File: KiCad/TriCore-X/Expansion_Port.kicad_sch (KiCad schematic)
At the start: 0 parts

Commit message: feat : add some Expansion Ports (work in progress)
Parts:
- added J2: 877159106, 877159106:CONN_87715-9106_MOL, symbol 877159106:877159106
- added J3: LPJG0926HENL, LPJG0926HENL:LINK-PP_LPJG0926HENL, symbol LPJG0926HENL:LPJG0926HENL
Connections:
- new net: J3.4 (CT), J3.5 (CT)
- new net: J3.S1 (SHIELD), J3.S2 (SHIELD)
- new net +12V: J2.A2, J2.A3, J2.B1, J2.B2, J2.B3
- new net GND: J2.A4, J2.B4

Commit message: refactor: change core MCU to STM32H723 and add LPDDR4/HDMI support
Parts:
- removed J3: LPJG0926HENL, LPJG0926HENL:LINK-PP_LPJG0926HENL, symbol LPJG0926HENL:LPJG0926HENL
- added D3: ESD224DQAR, ESD224DQAR:USON-10_L2.5-W1.0-P0.50-BL, symbol ESD224DQAR:ESD224DQAR
- added J3: HDMI_A, Connector_Video:HDMI_A_Molex_208658-1001_Horizontal, symbol Connector:HDMI_A
- added U1: RK3568B2, RK3568B2:BGA636C65P28X28_1900X1900X111, symbol RK3568B2:RK3568B2
- added U6: JFM38U1B-B313-4F, JFM38U1B-B313-4F:RJ45-TH_JFM38U11-B31X-4F, symbol JFM38U1B-B313-4F:JFM38U1B-B313-4F
- added U9: TPD12S016RKTR, TPD12S016RKTR:IC_TPD12S016RKTR, symbol TPD12S016RKTR:TPD12S016RKTR
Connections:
- net GND: now also U6.13 (GND), U6.16 (GND_DRAIN), U6.28 (GND), U6.4 (GND), U6.7 (GND_DRAIN), U9.13 (GND), U9.18 (GND), U9.5 (GND)
- new net HDMI_TX_AVDD_0V9: U1.V17 (HDMI_TX_AVDD_0V9), U1.V18 (HDMI_TX_AVDD_0V9)
- no-connect marks 0 -> 8

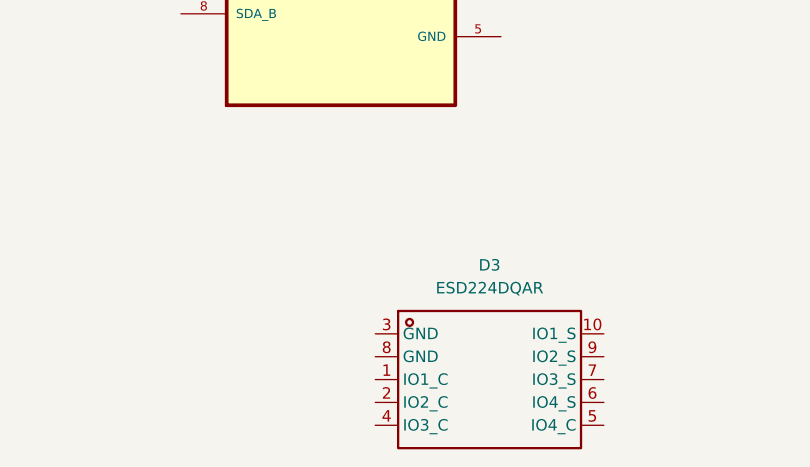
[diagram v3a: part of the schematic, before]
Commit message: feat: complete schematic for RK809-5 PMIC peripheral circuits
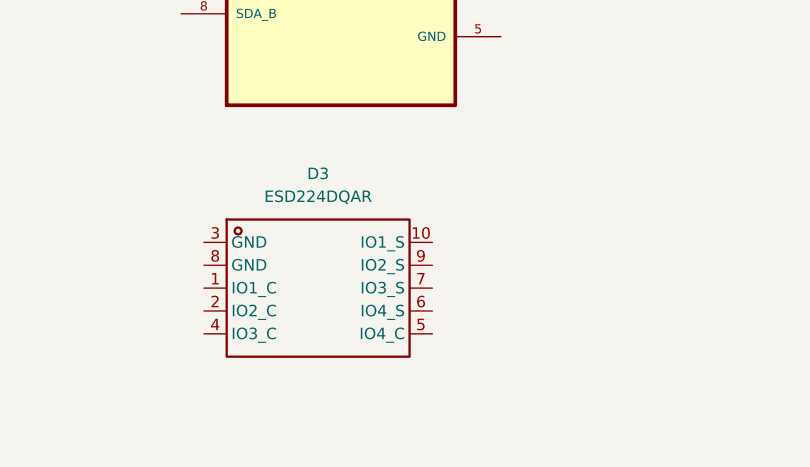
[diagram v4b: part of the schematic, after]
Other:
- moved on the sheet: D3
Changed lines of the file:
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@@
 	(symbol
 		(lib_id "ESD224DQAR:ESD224DQAR")
-		(at 466.09 138.43 0)
+		(at 447.04 128.27 0)
 		(unit 1)
 		(exclude_from_sim no)
@@
 		(fields_autoplaced yes)
 		(property "Reference" "D3"
-			(at 478.79 130.81 0)
+			(at 459.74 120.65 0)
 			(effects
 				(font
@@
 		)
 		(property "Value" "ESD224DQAR"
-			(at 478.79 133.35 0)
+			(at 459.74 123.19 0)
 			(effects
 				(font
@@
 		)
 		(property "Footprint" "ESD224DQAR:USON-10_L2.5-W1.0-P0.50-BL"
-			(at 478.79 156.21 0)
+			(at 459.74 146.05 0)
 			(effects
 				(font
@@
 		)
 		(property "Datasheet" ""
-			(at 466.09 138.43 0)
+			(at 447.04 128.27 0)
 			(effects
 				(font
@@
 		)
 		(property "Description" "ESD224DQAR"
-			(at 466.09 138.43 0)
+			(at 447.04 128.27 0)
 			(effects
 				(font
@@
 		)
 		(property "Manufacturer" "TI(德州仪器)"
-			(at 478.79 158.75 0)
+			(at 459.74 148.59 0)
 			(effects
 				(font
@@
 		)
 		(property "LCSC Part" "C1981316"
-			(at 478.79 161.29 0)
+			(at 459.74 151.13 0)
 			(effects
 				(font

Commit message: refactor: update schematic components and library references, including STM32H743 and new power symbols
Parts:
- removed J3: HDMI_A, Connector_Video:HDMI_A_Molex_208658-1001_Horizontal, symbol Connector:HDMI_A
- removed U1: RK3568B2, RK3568B2:BGA636C65P28X28_1900X1900X111, symbol RK3568B2:RK3568B2
- removed U6: JFM38U1B-B313-4F, JFM38U1B-B313-4F:RJ45-TH_JFM38U11-B31X-4F, symbol JFM38U1B-B313-4F:JFM38U1B-B313-4F
- removed U9: TPD12S016RKTR, TPD12S016RKTR:IC_TPD12S016RKTR, symbol TPD12S016RKTR:TPD12S016RKTR
- added C19: 1nF/50V, Capacitor_SMD:C_0402_1005Metric, symbol Device:C
- added C20, C21: 10nF, Capacitor_SMD:C_0402_1005Metric, symbol Device:C
- added C22, C25, C27: 100nF, Capacitor_SMD:C_0402_1005Metric, symbol Device:C
- added C23, C24: 15pF, Capacitor_SMD:C_0402_1005Metric, symbol Device:C
- added C26, C28: 10uF, Capacitor_SMD:C_0402_1005Metric, symbol Device:C
- added D4: ESD224DQAR, ESD224DQAR:USON-10_L2.5-W1.0-P0.50-BL, symbol ESD224DQAR:ESD224DQAR
- added D5: LESD5D5.0CT1G, LESD5D5.0CT1G:SOD-523_L1.2-W0.8-LS1.6-BI, symbol LESD5D5.0CT1G:LESD5D5.0CT1G
- added FB1: 220R@100M, Inductor_SMD:L_0603_1608Metric, symbol Device:FerriteBead
- added J3: HR911105A_C12074, RJ45:RJ45-TH_HR911105A, symbol RJ45:HR911105A_C12074
- added R16, R17: 510R, Resistor_SMD:R_0402_1005Metric, symbol Device:R
- added R18, R21, R22, R23, R29, R30: 4.7k, Resistor_SMD:R_0402_1005Metric, symbol Device:R
- added R19, R20: 1.5k, Resistor_SMD:R_0402_1005Metric, symbol Device:R
- added R24: 2.49k, Resistor_SMD:R_0402_1005Metric, symbol Device:R
- added R25, R26, R27, R28: 22R, Resistor_SMD:R_0402_1005Metric, symbol Device:R
- added U6: RTL8201F-VB-CG, RTL8201F-VB-CG:QFN-32_L5.0-W5.0-P0.50-BL-EP3.4, symbol RTL8201F-VB-CG:RTL8201F-VB-CG
- added USB1: AF 90° ZJDG ZB, USB-A:USB-A-TH_AF-90-ZJDG-ZB, symbol USB-A:AF 90° ZJDG ZB
- added Y1: 25Mhz, Crystal:Crystal_SMD_3225-4Pin_3.2x2.5mm, symbol Device:Crystal_GND24
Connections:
- net GND: now also C19.1, C20.1, C21.1, C22.2, C23.1, C24.1, C25.1, C26.2, C27.2, C28.2, D5.1, FB1.2, J3.11, R22.2, R23.2, R24.1, R30.1, U6.33 (EP), Y1.2 (G), Y1.4 (G)
- new net: C24.2, U6.31 (CKXTAL1), Y1.1
- new net: R28.2, U6.6 (MDI-[1])
- new net: C22.1, U6.29 (DVDD10OUT)
- new net: R25.2, U6.3 (MDI+[0])
- new net: C23.2, U6.32 (CKXTAL2), Y1.3
- new net: R27.2, U6.5 (MDI+[1])
- new net: C19.2, D5.2, J3.8 (CHSGND)
- new net: FB1.1, J3.SH1, J3.SH2
- new net: R24.2, U6.1 (RSET)
- new net: C25.2, U6.2 (AVDD10OUT)
- new net: J3.10, R16.2
- new net: J3.12, R17.2
- new net: C20.2, J3.4
- new net: C21.2, J3.5
- new net: R26.2, U6.4 (MDI-[0])
- new net: R29.2, U6.8 (RXDV)
- new net ETH_RX_N: J3.6 (RD-), R28.1
- new net ETH_RX_P: J3.3 (RD+), R27.1
- new net ETH_TX_N: J3.2 (TD-), R26.1
- new net ETH_TX_P: J3.1 (TD+), R25.1
- new net Ethernet_3V3: C26.1, C27.1, C28.1, J3.9, R18.2, R19.2, R20.2, R21.2, R29.1, U6.14 (DVDD33), U6.30 (AVDD33), U6.7 (AVDD33)
- new net LED_ACT: R16.1, R18.1, U6.24 (LED0/PHYAD[0]/PMEB)
- new net LED_LINK: R17.1, R23.1, U6.25 (LED1/PHYAD[1])
- new net PHY_CRS_DV: U6.26 (CRS/CRS_DV)
- new net PHY_MDC: R20.1, U6.22 (MDC)
- new net PHY_MDIO: R19.1, U6.23 (MDIO)
- new net PHY_RSTN: R21.1, U6.21 (PHYRSTB)
- new net PHY_RXD0: U6.9 (RXD[0])
- new net PHY_RXD1: R30.2, U6.10 (RXD[1])
- new net PHY_RXER: R22.1, U6.28 (RXER/FXEN)
- new net PHY_TXCLK: U6.15 (TXC)
- new net PHY_TXD0: U6.16 (TXD[0])
- new net PHY_TXD1: U6.17 (TXD[1])
- new net PHY_TXEN: U6.20 (TXEN)
- no-connect marks 8 -> 7

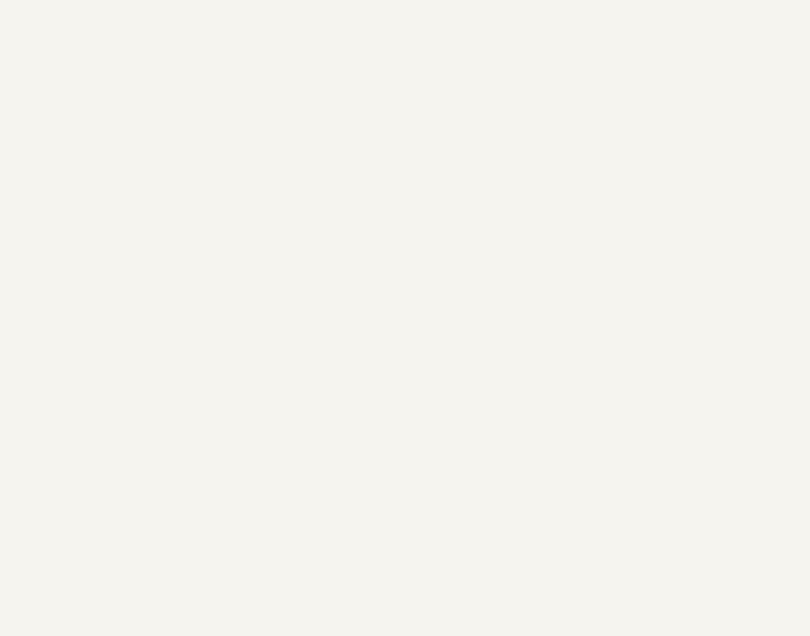
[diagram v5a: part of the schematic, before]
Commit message: refactor: update schematic components, remove unused files, and add new LED and CH334P symbols
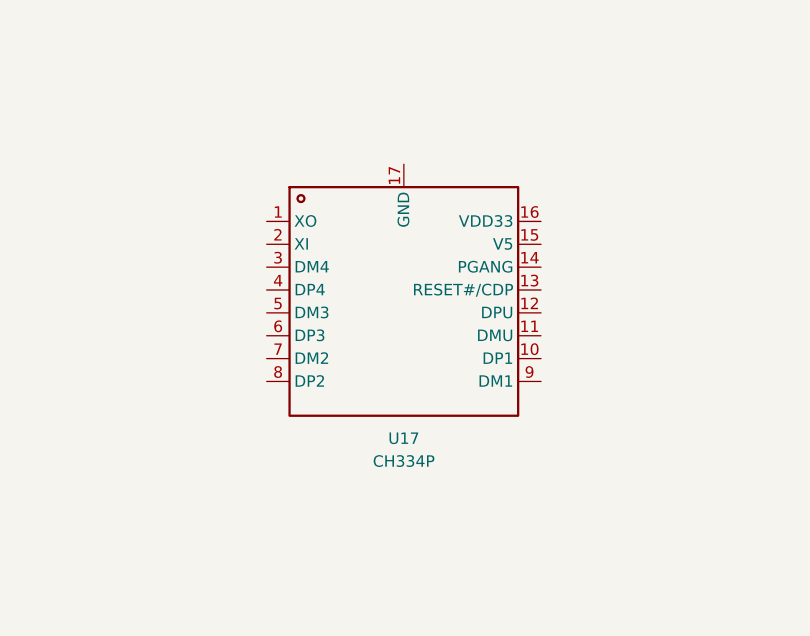
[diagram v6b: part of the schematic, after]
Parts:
- added U17: CH334P, CH334P:QFN-16_L3.0-W3.0-P0.50-BL-EP1.7, symbol CH334P:CH334P
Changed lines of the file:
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@@
+	)
+	(symbol
+		(lib_id "CH334P:CH334P")
+		(at 248.92 82.55 0)
+		(unit 1)
+		(exclude_from_sim no)
+		(in_bom yes)
+		(on_board yes)
+		(dnp no)
+		(fields_autoplaced yes)
+		(property "Reference" "U17"
+			(at 264.16 106.68 0)
+			(effects
+				(font
+					(size 1.27 1.27)
+				)
+			)
+		)
+		(property "Value" "CH334P"
+			(at 264.16 109.22 0)
+			(effects
+				(font
+					(size 1.27 1.27)
+				)
+			)
+		)
+		(property "Footprint" "CH334P:QFN-16_L3.0-W3.0-P0.50-BL-EP1.7"
+			(at 264.16 107.95 0)
+			(effects
+				(font
+					(size 1.27 1.27)
+				)
+				(hide yes)
+			)
+		)
+		(property "Datasheet" ""
+			(at 248.92 82.55 0)
+			(effects
+				(font
+					(size 1.27 1.27)
+				)
+				(hide yes)
+			)
+		)
+		(property "Description" "CH334P"
+			(at 248.92 82.55 0)
+			(effects
+				(font
+					(size 1.27 1.27)
+				)
+				(hide yes)
+			)
+		)
+		(property "Manufacturer" "WCH(南京沁恒)"
+			(at 264.16 110.49 0)
+			(effects
+				(font
+					(size 1.27 1.27)
+				)
+				(hide yes)
+			)
+		)
+		(property "LCSC Part" "C5373042"
+			(at 264.16 113.03 0)
+			(effects
+				(font
+					(size 1.27 1.27)
+				)
+				(hide yes)
+			)
+		)
+		(pin "12"
+		)
+		(pin "10"
+		)
+		(pin "13"
+		)
+		(pin "4"
+		)
+		(pin "14"
+		)
+		(pin "1"
+		)
+		(pin "2"
+		)
+		(pin "5"
+		)
+		(pin "6"
+		)
+		(pin "3"
+		)
+		(pin "7"
+		)
+		(pin "8"
+		)
+		(pin "17"
+		)
+		(pin "16"
+		)
+		(pin "15"
+		)
+		(pin "11"
+		)
+		(pin "9"
+		)
+		(instances
+			(project ""
+				(path "/b9ed8ff9-3a91-4311-b656-324fcf6f7e0c/0a747f2c-9f58-498b-af92-80cd731affd0"
+					(reference "U17")
+					(unit 1)
+				)
+			)
+		)
 	)
 	(symbol
